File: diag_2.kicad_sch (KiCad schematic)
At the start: 27 parts, among them CN2 JTAG-CONN2X3, IC3 XC9572XL-TQ100, P19 PINHD-1X1, P2 PINHD-1X1, P24 PINHD-1X1, P29 PINHD-1X1, P7 PINHD-1X1, P80 PINHD-1X1, P85 PINHD-1X1

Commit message: convert files to kicad, change to 4 layers and supplement decoupling
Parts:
- added C10, C8, C9: 0.01µf, Capacitor_SMD:C_0805_2012Metric, symbol diag-eagle-import:C-EU025-025X050
- C4, C5, C6, C7: footprint diag:C025-025X050 -> Capacitor_SMD:C_0805_2012Metric
- IC3: value XC9572XL-TQ100 -> XC95144XL-TQ100
- REG1B0: footprint diag:SOT223 -> PCM_Package_TO_SOT_SMD_AKL:SOT-223-3_TabPin2; symbol diag-eagle-import:LT1963EST -> PCM_Voltage_Regulator_AKL:LT1963EST-3.3
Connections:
- net GND: now also C10.2, C8.2, C9.2
- net VCC33: now also C10.1, C8.1, C9.1

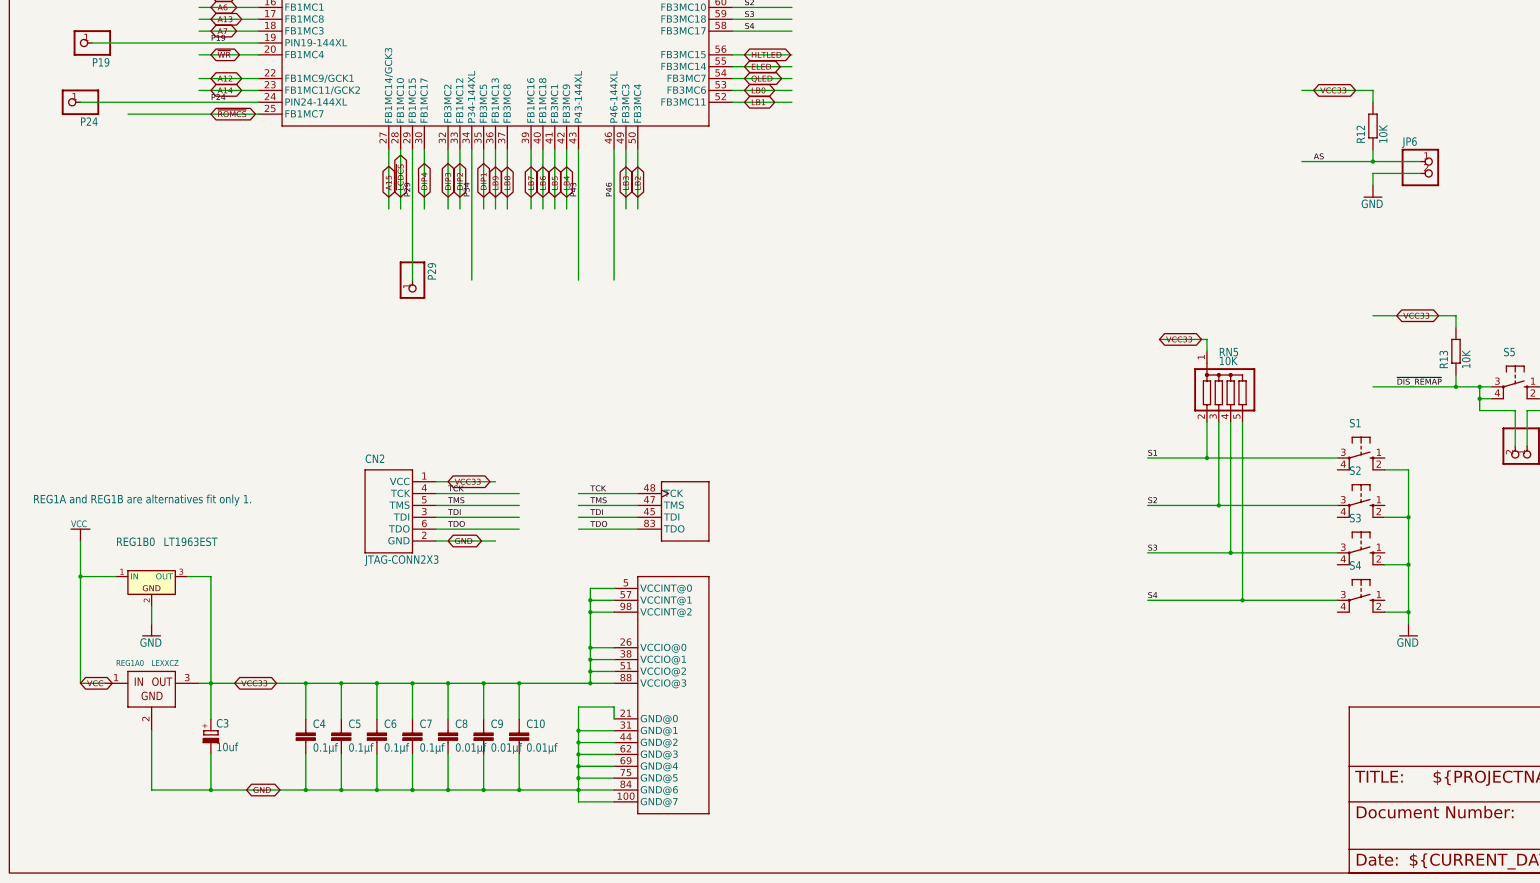
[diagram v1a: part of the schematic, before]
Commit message: convert more passives to smd
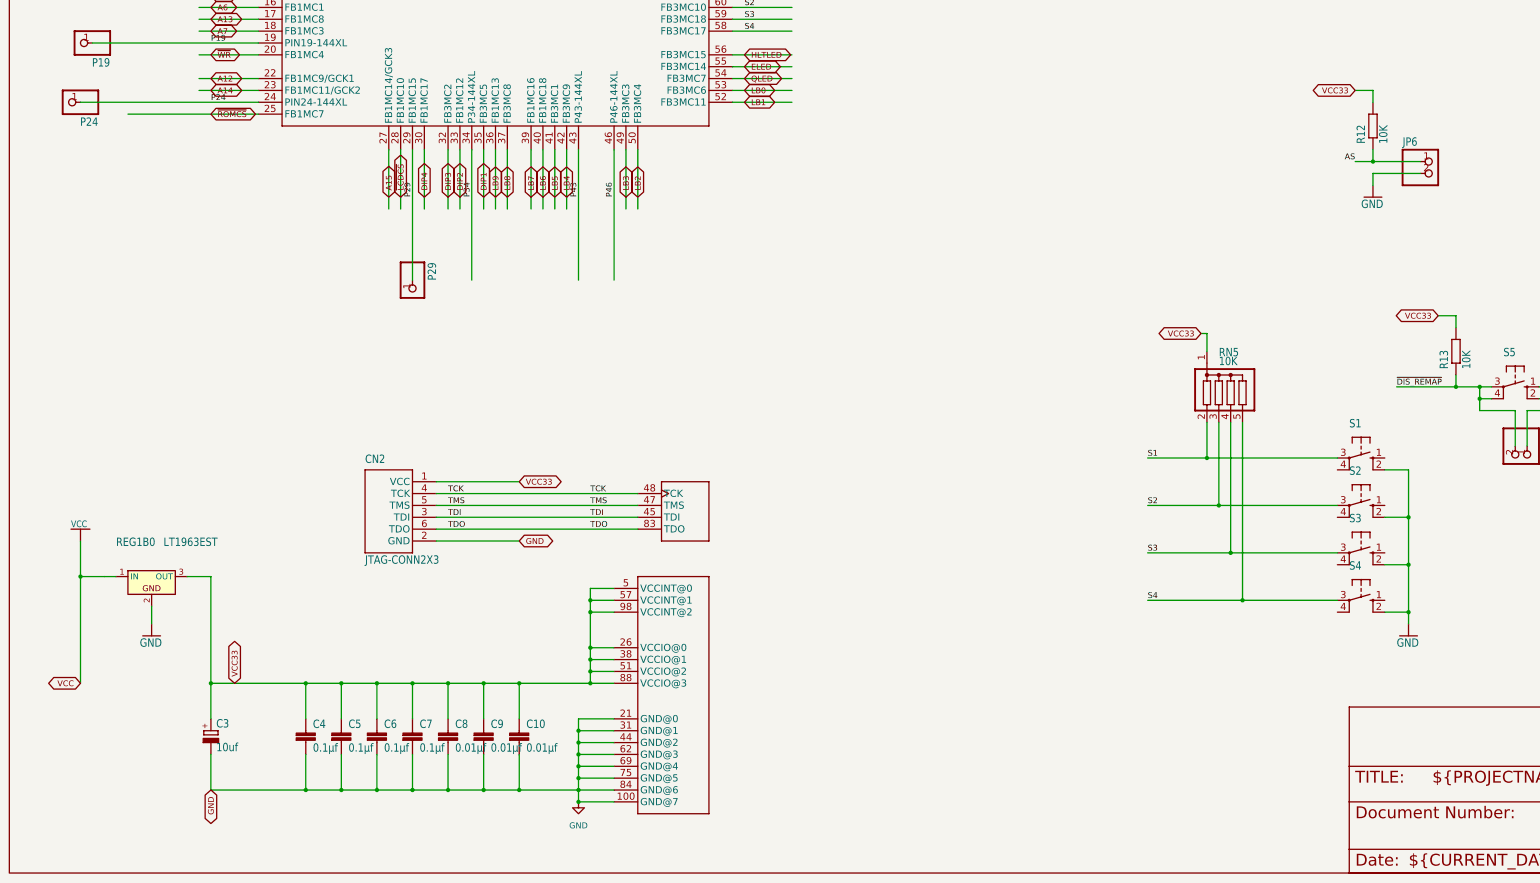
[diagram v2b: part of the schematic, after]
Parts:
- removed REG1A0: LEXXCZ, diag:TO92-, symbol diag-eagle-import:LEXXCZ
- R12, R13: footprint diag:0207_10 -> PCM_Resistor_SMD_AKL:R_0805_2012Metric
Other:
- note removed: "REG1A and REG1B are alternatives fit only 1."
